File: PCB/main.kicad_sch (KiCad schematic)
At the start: 59 parts, among them J1 S20B-PADSS-1, J2 S20B-PADSS-1, J3 SWD, SW1 SPST, U1 TPS54302, U2 XC6206P33, U3 TJA1051T/3, U4 TJA1051T/3, U5 STM32G0B1, Y1 ${Frequency}

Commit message: Generate output files
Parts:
- C13, C14: symbol 0 Passive_Components:Capacitors/CMP-0005 -> 0 Passive_Components:Capacitors/CMP-0072; Capacitance 15p -> 27p; LCSC C1548 -> C1557; MPN 0402CG150J500NT -> 0402CG270J500NT
- Y1: footprint libdb:CMP-0004 -> Crystal:Crystal_SMD_3225-4Pin_3.2x2.5mm; symbol 0 Passive_Components:Crystals/CMP-0004 -> 0 Passive_Components:Crystals/CMP-0071; LCSC C485379 -> C9010; Load Capacitance 8p -> 15p; MPN NX2016SA-40M-STD-CZS-3 -> X322540MPB4SI; Manufacturer NDK -> Yangxing Tech
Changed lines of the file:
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@@
   (junction (at 49.53 74.295) (diameter 0) (color 0 0 0 0)
   )
-  (junction (at 200.66 114.3) (diameter 0) (color 0 0 0 0)
-  )
   (junction (at 242.57 48.26) (diameter 0) (color 0 0 0 0)
   )
@@
   (junction (at 143.51 59.055) (diameter 0) (color 0 0 0 0)
   )
+  (junction (at 200.66 114.3) (diameter 0) (color 0 0 0 0)
+  )
   (junction (at 199.39 71.12) (diameter 0) (color 0 0 0 0)
   )
@@
     (stroke (width 0) (type default))
   )
+  (wire (pts (xy 200.66 114.3) (xy 207.01 114.3))
+    (stroke (width 0) (type default))
+  )
   (wire (pts (xy 45.72 186.69) (xy 59.69 186.69))
     (stroke (width 0) (type default))
@@
     (stroke (width 0) (type default))
   )
-  (wire (pts (xy 200.66 114.3) (xy 207.01 114.3))
-    (stroke (width 0) (type default))
-  )
   (wire (pts (xy 266.7 124.46) (xy 278.13 124.46))
     (stroke (width 0) (type default))
@@
     (stroke (width 0) (type default))
   )
-  (wire (pts (xy 200.66 113.03) (xy 200.66 114.3))
-    (stroke (width 0) (type default))
-  )
   (wire (pts (xy 260.35 96.52) (xy 278.13 96.52))
     (stroke (width 0) (type default))
@@
     (stroke (width 0) (type default))
   )
+  (wire (pts (xy 200.66 113.03) (xy 200.66 114.3))
+    (stroke (width 0) (type default))
+  )
   (wire (pts (xy 45.72 148.59) (xy 59.69 148.59))
     (stroke (width 0) (type default))
@@
     )
   )
-  (symbol (lib_id "0 Passive_Components:Crystals/CMP-0004") (at 207.01 106.68 0) (unit 1)
+  (symbol (lib_id "0 Passive_Components:Crystals/CMP-0071") (at 207.01 106.68 0) (unit 1)
     (in_bom yes) (on_board yes) (dnp no)
     (property "Reference" "Y1" (at 209.55 99.06 0)
       (effects (font (size 1.27 1.27)))
     )
-    (property "Value" "${Frequency}" (at 209.55 101.6 0)
-      (effects (font (size 1.27 1.27)))
+    (property "Value" "${Frequency}" (at 208.28 101.6 0)
+      (effects (font (size 1.27 1.27)) (justify left))
     )
-    (property "Footprint" "libdb:CMP-0004" (at 207.01 106.68 0)
+    (property "Footprint" "Crystal:Crystal_SMD_3225-4Pin_3.2x2.5mm" (at 207.01 106.68 0)
       (effects (font (size 1.27 1.27)) hide)
     )
@@
       (effects (font (size 1.27 1.27)) hide)
     )
-    (property "Manufacturer" "NDK " (at 207.01 106.68 0)
+    (property "Manufacturer" "Yangxing Tech" (at 207.01 106.68 0)
       (effects (font (size 1.27 1.27)) hide)
     )
-    (property "MPN" "NX2016SA-40M-STD-CZS-3" (at 207.01 106.68 0)
+    (property "MPN" "X322540MPB4SI" (at 207.01 106.68 0)
       (effects (font (size 1.27 1.27)) hide)
     )
@@
       (effects (font (size 1.27 1.27)) hide)
     )
-    (property "Load Capacitance" "8p" (at 207.01 106.68 0)
+    (property "Load Capacitance" "15p" (at 207.01 106.68 0)
       (effects (font (size 1.27 1.27)) hide)
     )
@@
       (effects (font (size 1.27 1.27)) hide)
     )
-    (property "LCSC" "C485379" (at 207.01 106.68 0) (show_name)
+    (property "LCSC" "C9010" (at 207.01 106.68 0) (show_name)
       (effects (font (size 1.27 1.27)) hide)
     )
@@
     )
   )
-  (symbol (lib_id "0 Passive_Components:Capacitors/CMP-0005") (at 200.66 110.49 0) (mirror y) (unit 1)
+  (symbol (lib_id "0 Passive_Components:Capacitors/CMP-0072") (at 200.66 110.49 0) (mirror y) (unit 1)
     (in_bom yes) (on_board yes) (dnp no)
-    (property "Reference" "C13" (at 196.85 109.22 0)
-      (effects (font (size 1.27 1.27)))
+    (property "Reference" "C13" (at 198.755 108.585 0)
+      (effects (font (size 1.27 1.27)) (justify left))
     )
-    (property "Value" "${Capacitance}" (at 196.85 111.76 0)
+    (property "Value" "${Capacitance}" (at 196.85 110.49 0)
       (effects (font (size 1.27 1.27)))
     )
@@
       (effects (font (size 1.27 1.27)) hide)
     )
-    (property "MPN" "0402CG150J500NT" (at 200.66 110.49 0)
+    (property "MPN" "0402CG270J500NT" (at 200.66 110.49 0)
       (effects (font (size 1.27 1.27)) hide)
     )
-    (property "Capacitance" "15p" (at 200.66 110.49 0)
+    (property "Capacitance" "27p" (at 200.66 110.49 0)
       (effects (font (size 1.27 1.27)) hide)
     )
-    (property "Capacitance Tolerance" "5%" (at 191.77 110.49 90)
+    (property "Capacitance Tolerance" "5%" (at 200.66 110.49 0)
       (effects (font (size 1.27 1.27)) hide)
     )
-    (property "Voltage Rating" "50V" (at 191.77 110.49 90)
-      (effects (font (size 1.27 1.27)) hide)
+    (property "Voltage Rating" "50V" (at 196.85 112.395 0)
+      (effects (font (size 1.27 1.27)))
     )
     (property "Dielectric" "C0G" (at 200.66 110.49 0)
       (effects (font (size 1.27 1.27)) hide)
     )
-    (property "Case Package Size" "0402" (at 186.69 110.49 90)
+    (property "Case Package Size" "0402" (at 200.66 110.49 0)
       (effects (font (size 1.27 1.27)) hide)
     )
-    (property "LCSC" "C1548" (at 200.66 110.49 0) (show_name)
+    (property "LCSC" "C1557" (at 200.66 110.49 0) (show_name)
       (effects (font (size 1.27 1.27)) hide)
     )
@@
     )
   )
-  (symbol (lib_id "0 Passive_Components:Capacitors/CMP-0005") (at 213.36 110.49 0) (unit 1)
+  (symbol (lib_id "0 Passive_Components:Capacitors/CMP-0072") (at 213.36 110.49 0) (unit 1)
     (in_bom yes) (on_board yes) (dnp no)
-    (property "Reference" "C14" (at 217.17 109.22 0)
-      (effects (font (size 1.27 1.27)))
+    (property "Reference" "C14" (at 215.265 108.585 0)
+      (effects (font (size 1.27 1.27)) (justify left))
     )
-    (property "Value" "${Capacitance}" (at 217.17 111.76 0)
+    (property "Value" "${Capacitance}" (at 217.17 110.49 0)
       (effects (font (size 1.27 1.27)))
     )
@@
       (effects (font (size 1.27 1.27)) hide)
     )
-    (property "MPN" "0402CG150J500NT" (at 213.36 110.49 0)
+    (property "MPN" "0402CG270J500NT" (at 213.36 110.49 0)
       (effects (font (size 1.27 1.27)) hide)
     )
-    (property "Capacitance" "15p" (at 213.36 110.49 0)
+    (property "Capacitance" "27p" (at 213.36 110.49 0)
       (effects (font (size 1.27 1.27)) hide)
     )
-    (property "Capacitance Tolerance" "5%" (at 222.25 110.49 90)
+    (property "Capacitance Tolerance" "5%" (at 213.36 110.49 0)
       (effects (font (size 1.27 1.27)) hide)
     )
-    (property "Voltage Rating" "50V" (at 217.17 110.49 90)
-      (effects (font (size 1.27 1.27)) hide)
+    (property "Voltage Rating" "50V" (at 217.17 112.395 0)
+      (effects (font (size 1.27 1.27)))
     )
     (property "Dielectric" "C0G" (at 213.36 110.49 0)
       (effects (font (size 1.27 1.27)) hide)
     )
-    (property "Case Package Size" "0402" (at 217.17 110.49 90)
+    (property "Case Package Size" "0402" (at 213.36 110.49 0)
       (effects (font (size 1.27 1.27)) hide)
     )
-    (property "LCSC" "C1548" (at 213.36 110.49 0) (show_name)
+    (property "LCSC" "C1557" (at 213.36 110.49 0) (show_name)
       (effects (font (size 1.27 1.27)) hide)
     )

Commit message: Change switch
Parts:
- removed SW1: SPST, libdb:CMP-0011, symbol 0 Electromechanical:Tactile Switches/CMP-0011
- added SW1: Tactile, libdb:CMP-0072, symbol 0 Electromechanical:Tactile Switches/CMP-0073
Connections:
- net GND: now also SW1.2
- net at C15.1, U5.10 (PF2): now also SW1.1
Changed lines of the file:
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@@
-    )
-  )
-  (symbol (lib_id "0 Electromechanical:Tactile Switches/CMP-0011") (at 187.96 77.47 270) (mirror x) (unit 1)
-    (in_bom yes) (on_board yes) (dnp no)
-    (property "Reference" "SW1" (at 182.245 76.2 90)
-      (effects (font (size 1.27 1.27)) (justify left))
-    )
-    (property "Value" "SPST" (at 182.245 78.74 90)
-      (effects (font (size 1.27 1.27)) (justify left))
-    )
-    (property "Footprint" "libdb:CMP-0011" (at 193.04 77.47 0)
-      (effects (font (size 1.27 1.27)) hide)
-    )
-    (property "Datasheet" "~" (at 193.04 77.47 0)
-      (effects (font (size 1.27 1.27)) hide)
-    )
-    (property "Manufacturer" "XKB Connectivity" (at 187.96 77.47 0)
-      (effects (font (size 1.27 1.27)) hide)
-    )
-    (property "MPN" "TS-1187A-B-A-B" (at 187.96 77.47 0)
-      (effects (font (size 1.27 1.27)) hide)
-    )
-    (property "LCSC" "C318884" (at 187.96 77.47 0) (show_name)
-      (effects (font (size 1.27 1.27)) hide)
-    )
-    (pin "1")
-    (pin "2")
-    (instances
-      (project "main"
-        (path "/4f4cf64f-c95a-4a4a-b388-e87470ab2a3e"
-          (reference "SW1") (unit 1)
-        )
-      )
     )
   )
@@
         )
       )
+    )
+  )
+  (symbol (lib_id "0 Electromechanical:Tactile Switches/CMP-0073") (at 187.96 77.47 270) (unit 1)
+    (in_bom yes) (on_board yes) (dnp no)
+    (property "Reference" "SW1" (at 186.69 76.2 90)
+      (effects (font (size 1.27 1.27)) (justify right))
+    )
+    (property "Value" "Tactile" (at 186.69 78.74 90)
+      (effects (font (size 1.27 1.27)) (justify right))
+    )
+    (property "Footprint" "libdb:CMP-0072" (at 193.04 77.47 0)
+      (effects (font (size 1.27 1.27)) hide)
+    )
+    (property "Datasheet" "~" (at 193.04 77.47 0)
+      (effects (font (size 1.27 1.27)) hide)
+    )
+    (property "Manufacturer" "C&K" (at 187.96 77.47 0)
+      (effects (font (size 1.27 1.27)) hide)
+    )
+    (property "MPN" "PTS810SJK250SMTRLFS" (at 187.96 77.47 0)
+      (effects (font (size 1.27 1.27)) hide)
+    )
+    (property "LCSC" "C221896" (at 187.96 77.47 0) (show_name)
+      (effects (font (size 1.27 1.27)) hide)
+    )
+    (pin "1")
+    (pin "2")
+    (instances
+      (project "main"
+        (path "/4f4cf64f-c95a-4a4a-b388-e87470ab2a3e"
+          (reference "SW1") (unit 1)
+        )
+      )

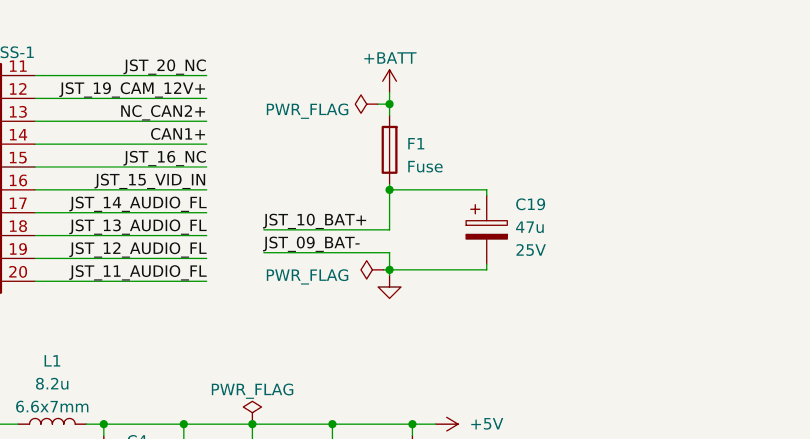
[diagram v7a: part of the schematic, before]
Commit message: Change fuse and adjust board size
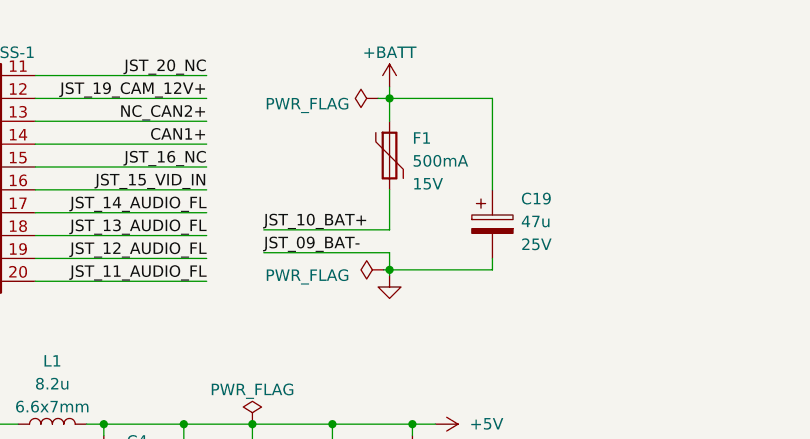
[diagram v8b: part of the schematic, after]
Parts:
- removed F1: Fuse, libdb:CMP-0026, symbol 0 Circuit_Protection:Fuse Holders/CMP-0026
- added F1: 500mA, libdb:CMP-0076, symbol 0 Circuit_Protection:Poly Fuses/CMP-0076
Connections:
- net +BATT: now also C19.1, F1.1
- net JST_10_BAT+: now also F1.2; no longer C19.1
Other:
- moved on the sheet: C19
